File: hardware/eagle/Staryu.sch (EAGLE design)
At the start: 28 parts, among them SW1 CHERRY-MX-LED, SW2 CHERRY-MX-LED, SW3 CHERRY-MX-LED, SW4 CHERRY-MX-LED, SW5 CHERRY-MX-LED, U1 ATMEGA32U2-TQFP, Y1 16MHZ

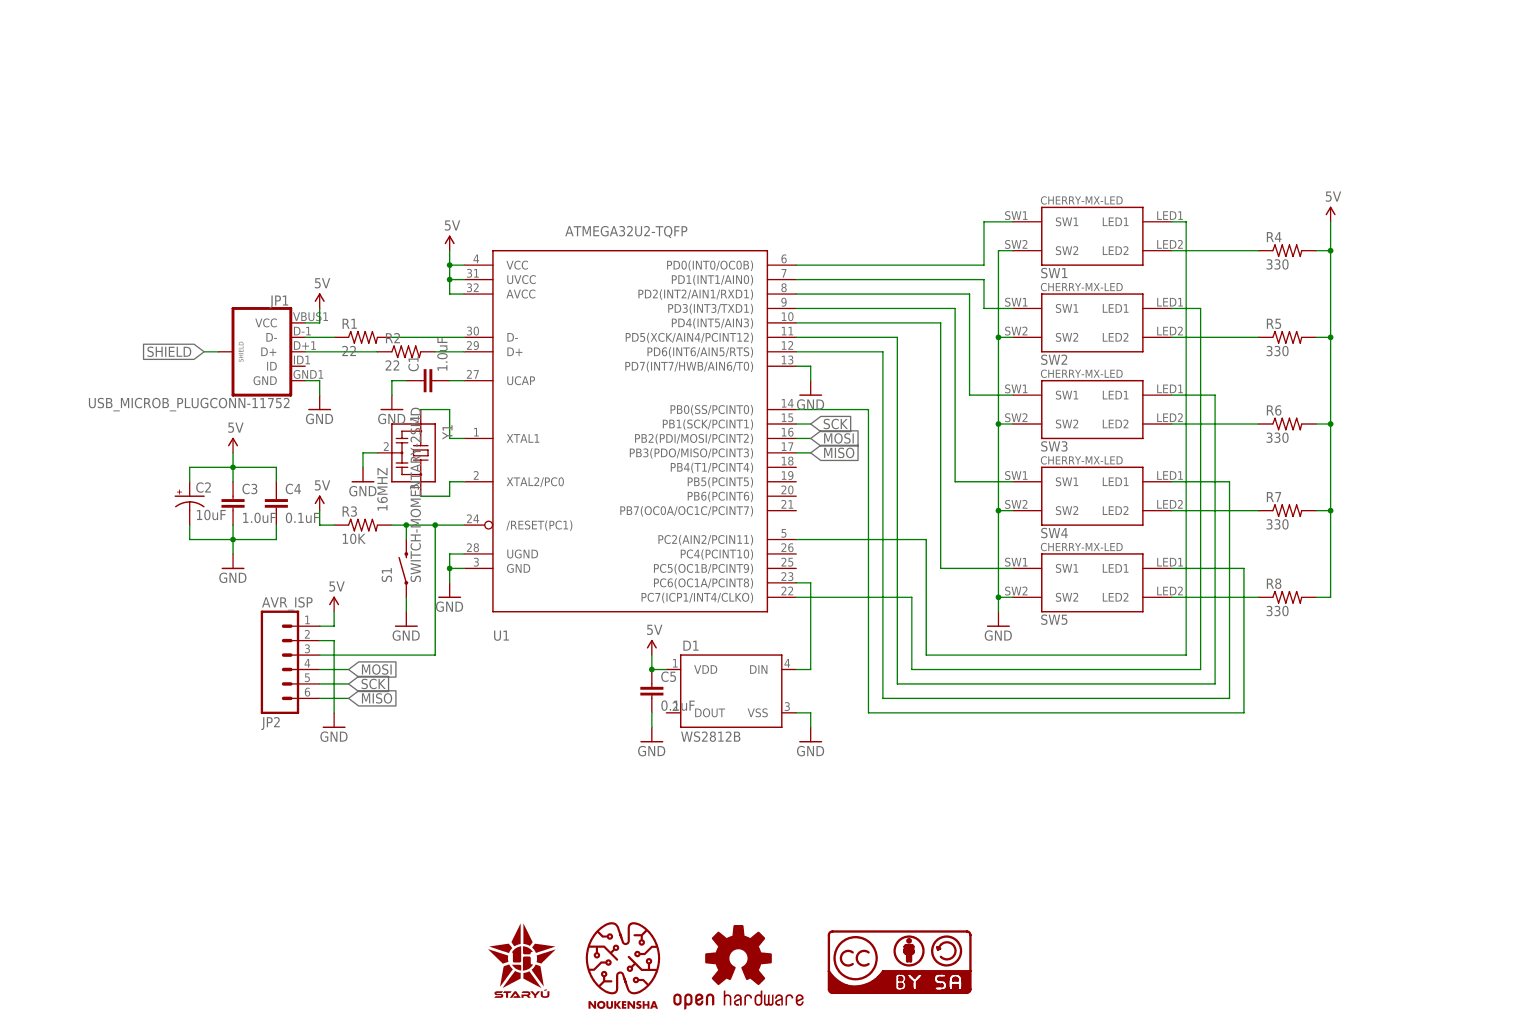
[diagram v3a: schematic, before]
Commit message: Update hardware to v1.4 - Support both of ATMEGA32U2-AU (32-TQFP) and ATMEGA32U2-MU (32-QFN) - Support both of normal and reverse mounting switch (selected by jumper) - Replace Micro USB connector with a much tougher one - Add a new DOUT connector exported from WS2812B - Correct name and value of Y1 - Change logo
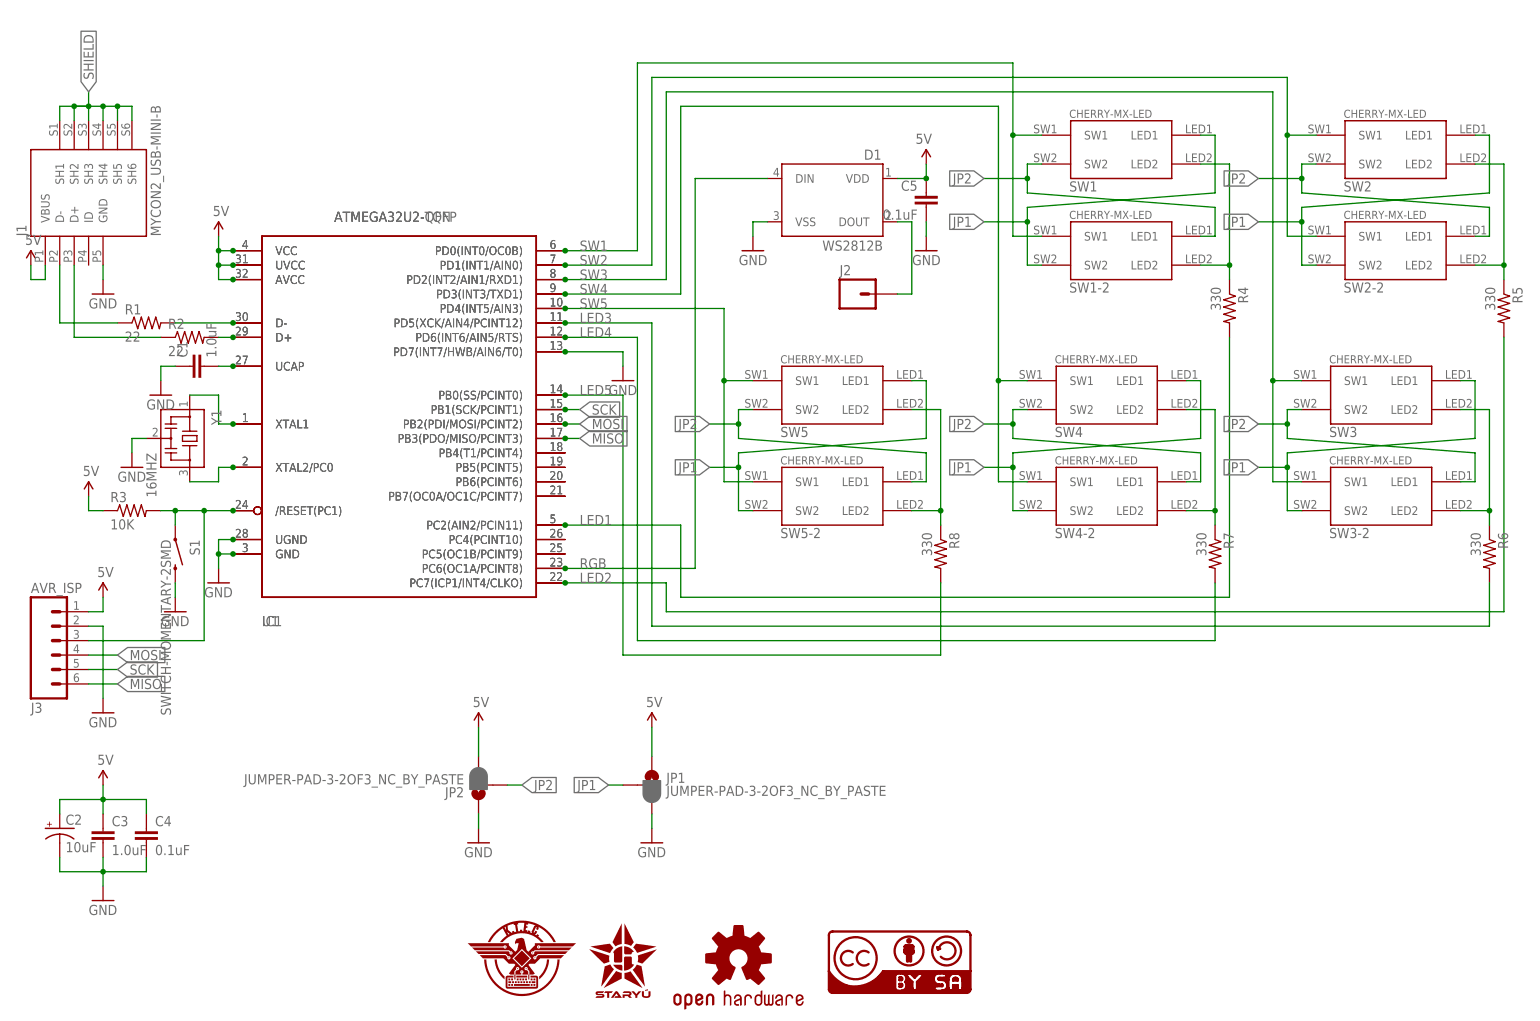
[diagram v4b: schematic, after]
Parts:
- removed LOGO2: NOUKENSHA_LOGO.3_EXP, Noukensha:NOUKENSHA_LOGO.3_EXP
- added IC1: ATMEGA32U2-QFN, atmega32u2:ATMEGA32U2-QFN
- added J1: MYCON2_USB-MINI-B, usb-micro-b:MYCON2_USB-MINI-B
- added J2: (no value), SparkFun-Connectors:M01PTH_NO_SILK_YES_STOP
- added J3: AVR_ISP, SparkFun-Connectors:M06NO_SILK_FEMALE_PTH
- added SW1-2, SW2-2, SW3-2, SW4-2, SW5-2: CHERRY-MX-LED-MOD, cherrymx:CHERRY-MX-LED-MOD
- added U$1: K.T.E.C._LOGO.3_INCH_EXP, logo:K.T.E.C._LOGO.3_INCH_EXP
- C1, C3: device SparkFun-Capacitors:CAP0805 -> SparkFun-Capacitors:1.0UF-25V-+80/-20(0805)"
- JP1: value USB_MICROB_PLUGCONN-11752 -> JUMPER-PAD-3-2OF3_NC_BY_PASTE; device SparkFun-Connectors:USB_MICROB_PLUGCONN-11752 -> SparkFun-Passives:JUMPER-PAD-3-2OF3_NC_BY_PASTE
- JP2: value AVR_ISP -> JUMPER-PAD-3-2OF3_NC_BY_PASTE; device SparkFun-Connectors:M06NO_SILK_FEMALE_PTH -> SparkFun-Passives:JUMPER-PAD-3-2OF3_NC_BY_PASTE
- SW1, SW2, SW3, SW4, SW5: value CHERRY-MX-LED -> CHERRY-MX-LED-MOD; device cherrymx:CHERRY-MX-LED -> cherrymx:CHERRY-MX-LED-MOD
- U1: device adafruit:ATMEGA32U2-TQFP -> atmega32u2:ATMEGA32U2-TQFP
- Y1: device cstce-resonator:CSTCR6M00G53Z -> cst-resonator:CSTCE16M0V53-R0
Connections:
- removed net N$14: SW1.SW1, U1.PD0(INT0/OC0B)
- removed net N$15: SW2.SW1, U1.PD1(INT1/AIN0)
- removed net N$16: SW3.SW1, U1.PD2(INT2/AIN1/RXD1)
- removed net N$17: SW4.SW1, U1.PD3(INT3/TXD1)
- removed net N$18: SW5.SW1, U1.PD4(INT5/AIN3)
- removed net N$19: D1.DIN, U1.PC6(OC1A/PCINT8)
- removed net N$30: SW4.LED1, U1.PD6(INT6/AIN5/RTS)
- removed net N$31: SW2.LED1, U1.PC7(ICP1/INT4/CLKO)
- removed net N$32: SW3.LED1, U1.PD5(XCK/AIN4/PCINT12)
- removed net N$33: SW5.LED1, U1.PB0(SS/PCINT0)
- removed net N$34: SW1.LED1, U1.PC2(AIN2/PCIN11)
- new net JP1: JP1.2, SW1-2.SW2, SW1.LED1, SW2-2.SW2, SW2.LED1, SW3-2.SW2, SW3.LED1, SW4-2.SW2, SW4.LED1, SW5-2.SW2, SW5.LED1
- new net JP2: JP2.2, SW1-2.LED1, SW1.SW2, SW2-2.LED1, SW2.SW2, SW3-2.LED1, SW3.SW2, SW4-2.LED1, SW4.SW2, SW5-2.LED1, SW5.SW2
- new net LED1: IC1.PC2(AIN2/PCIN11), R4.2, U1.PC2(AIN2/PCIN11)
- new net LED2: IC1.PC7(ICP1/INT4/CLKO), R5.2, U1.PC7(ICP1/INT4/CLKO)
- new net LED3: IC1.PD5(XCK/AIN4/PCINT12), R6.2, U1.PD5(XCK/AIN4/PCINT12)
- new net LED4: IC1.PD6(INT6/AIN5/RTS), R7.2, U1.PD6(INT6/AIN5/RTS)
- new net LED5: IC1.PB0(SS/PCINT0), R8.2, U1.PB0(SS/PCINT0)
- new net N$20: IC1.PB4(T1/PCINT4), U1.PB4(T1/PCINT4)
- new net N$21: IC1.PB5(PCINT5), U1.PB5(PCINT5)
- new net N$22: IC1.PB6(PCINT6), U1.PB6(PCINT6)
- new net N$23: IC1.PB7(OC0A/OC1C/PCINT7), U1.PB7(OC0A/OC1C/PCINT7)
- new net N$24: IC1.PC4(PCINT10), U1.PC4(PCINT10)
- new net N$25: IC1.PC5(OC1B/PCINT9), U1.PC5(OC1B/PCINT9)
- new net N$29: R4.1, SW1-2.LED2, SW1.LED2
- new net RGB: D1.DIN, IC1.PC6(OC1A/PCINT8), U1.PC6(OC1A/PCINT8)
- new net SW1: IC1.PD0(INT0/OC0B), SW1-2.SW1, SW1.SW1, U1.PD0(INT0/OC0B)
- new net SW2: IC1.PD1(INT1/AIN0), SW2-2.SW1, SW2.SW1, U1.PD1(INT1/AIN0)
- new net SW3: IC1.PD2(INT2/AIN1/RXD1), SW3-2.SW1, SW3.SW1, U1.PD2(INT2/AIN1/RXD1)
- new net SW4: IC1.PD3(INT3/TXD1), SW4-2.SW1, SW4.SW1, U1.PD3(INT3/TXD1)
- new net SW5: IC1.PD4(INT5/AIN3), SW5-2.SW1, SW5.SW1, U1.PD4(INT5/AIN3)
- net 5V: now also IC1.AVCC, IC1.UVCC, IC1.VCC, J1.VBUS, J3.1, JP1.1, JP2.3; no longer JP1.VCC, JP2.1, R4.2, R5.2, R6.2, R7.2, R8.2
- net GND: now also IC1.GND, IC1.PD7(INT7/HWB/AIN6/T0), IC1.UGND, J1.GND, J3.2, JP1.3, JP2.1, S1.2; no longer JP1.GND, JP2.2, S1.1, SW1.SW2, SW2.SW2, SW3.SW2, SW4.SW2, SW5.SW2
- net MISO: now also IC1.PB3(PDO/MISO/PCINT3), J3.6; no longer JP2.6
- net MOSI: now also IC1.PB2(PDI/MOSI/PCINT2), J3.4; no longer JP2.4
- net N$1: now also IC1.D+
- net N$10: now also SW2-2.LED2
- net N$11: now also SW3-2.LED2
- net N$12: now also SW4-2.LED2
- net N$13: now also SW5-2.LED2
- net N$2: now also IC1.D-
- net N$3: now also J1.D-; no longer JP1.D-
- net N$4: now also J1.D+; no longer JP1.D+
- net N$5: now also IC1.XTAL1
- net N$6: now also IC1.XTAL2/PC0
- net N$7: now also IC1.UCAP
- net N$8: now also IC1./RESET(PC1), J3.3, S1.1; no longer JP2.3, S1.2
- net N$9: now also D1.DOUT, J2.1; no longer R4.1, SW1.LED2
- net SCK: now also IC1.PB1(SCK/PCINT1), J3.5; no longer JP2.5
- net SHIELD: now also J1.SH1, J1.SH2, J1.SH3, J1.SH4, J1.SH5, J1.SH6; no longer JP1.SHIELD
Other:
- moved on the sheet: C1, C2, C3, C4, C5, D1, R1, R2, R3, R4, R5, R6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

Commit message: Update hardware to v1.5 - Improve jumpers for selecting switch mounting - Change logo
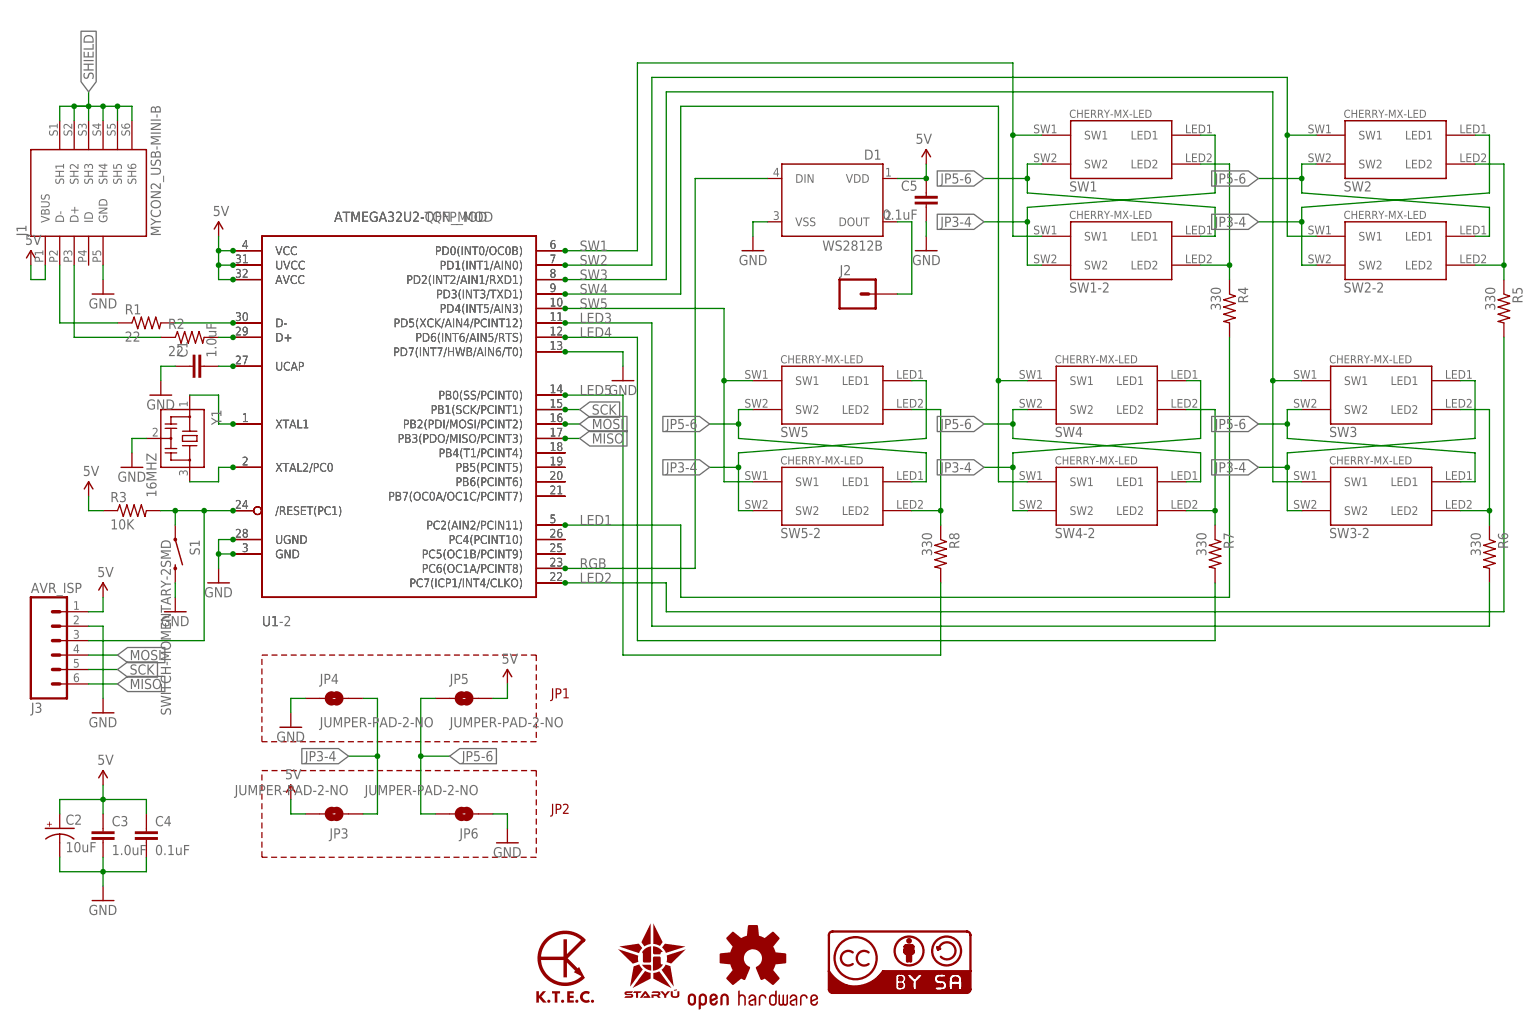
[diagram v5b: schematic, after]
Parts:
- removed IC1: ATMEGA32U2-QFN, atmega32u2:ATMEGA32U2-QFN
- removed JP1, JP2: JUMPER-PAD-3-2OF3_NC_BY_PASTE, SparkFun-Passives:JUMPER-PAD-3-2OF3_NC_BY_PASTE
- removed U$1: K.T.E.C._LOGO.3_INCH_EXP, logo:K.T.E.C._LOGO.3_INCH_EXP
- added JP3, JP4, JP5, JP6: JUMPER-PAD-2-NO, SparkFun-Passives:JUMPER-PAD-2-NO
- added LOGO2: STARYU_LOGO, Noukensha:STARYU_LOGO
- added U1-2: ATMEGA32U2-QFN_MOD, atmega32u2:ATMEGA32U2-QFN_MOD
- LOGO1: value STARYU_LOGO -> K.T.E.C._LOGO3_COPPER_EXP_S; device Noukensha:STARYU_LOGO -> logo:K.T.E.C._LOGO3_COPPER_EXP_S
- U1: value ATMEGA32U2-TQFP -> ATMEGA32U2-TQFP_MOD; device atmega32u2:ATMEGA32U2-TQFP -> atmega32u2:ATMEGA32U2-TQFP_MOD
- renumbered U$3 to LOGO4
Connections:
- removed net JP1: JP1.2, SW1-2.SW2, SW1.LED1, SW2-2.SW2, SW2.LED1, SW3-2.SW2, SW3.LED1, SW4-2.SW2, SW4.LED1, SW5-2.SW2, SW5.LED1
- removed net JP2: JP2.2, SW1-2.LED1, SW1.SW2, SW2-2.LED1, SW2.SW2, SW3-2.LED1, SW3.SW2, SW4-2.LED1, SW4.SW2, SW5-2.LED1, SW5.SW2
- new net JP3-4: JP3.1, JP4.2, SW1-2.SW2, SW1.LED1, SW2-2.SW2, SW2.LED1, SW3-2.SW2, SW3.LED1, SW4-2.SW2, SW4.LED1, SW5-2.SW2, SW5.LED1
- new net JP5-6: JP5.1, JP6.2, SW1-2.LED1, SW1.SW2, SW2-2.LED1, SW2.SW2, SW3-2.LED1, SW3.SW2, SW4-2.LED1, SW4.SW2, SW5-2.LED1, SW5.SW2
- net 5V: now also JP3.2, JP5.2, U1-2.AVCC, U1-2.UVCC, U1-2.VCC; no longer IC1.AVCC, IC1.UVCC, IC1.VCC, JP1.1, JP2.3
- net GND: now also JP4.1, JP6.1, U1-2.GND, U1-2.PD7(INT7/HWB/AIN6/T0), U1-2.UGND; no longer IC1.GND, IC1.PD7(INT7/HWB/AIN6/T0), IC1.UGND, JP1.3, JP2.1
- net LED1: now also U1-2.PC2(AIN2/PCIN11); no longer IC1.PC2(AIN2/PCIN11)
- net LED2: now also U1-2.PC7(ICP1/INT4/CLKO); no longer IC1.PC7(ICP1/INT4/CLKO)
- net LED3: now also U1-2.PD5(XCK/AIN4/PCINT12); no longer IC1.PD5(XCK/AIN4/PCINT12)
- net LED4: now also U1-2.PD6(INT6/AIN5/RTS); no longer IC1.PD6(INT6/AIN5/RTS)
- net LED5: now also U1-2.PB0(SS/PCINT0); no longer IC1.PB0(SS/PCINT0)
- net MISO: now also U1-2.PB3(PDO/MISO/PCINT3); no longer IC1.PB3(PDO/MISO/PCINT3)
- net MOSI: now also U1-2.PB2(PDI/MOSI/PCINT2); no longer IC1.PB2(PDI/MOSI/PCINT2)
- net N$1: now also U1-2.D+; no longer IC1.D+
- net N$2: now also U1-2.D-; no longer IC1.D-
- net N$20: now also U1-2.PB4(T1/PCINT4); no longer IC1.PB4(T1/PCINT4)
- net N$21: now also U1-2.PB5(PCINT5); no longer IC1.PB5(PCINT5)
- net N$22: now also U1-2.PB6(PCINT6); no longer IC1.PB6(PCINT6)
- net N$23: now also U1-2.PB7(OC0A/OC1C/PCINT7); no longer IC1.PB7(OC0A/OC1C/PCINT7)
- net N$24: now also U1-2.PC4(PCINT10); no longer IC1.PC4(PCINT10)
- net N$25: now also U1-2.PC5(OC1B/PCINT9); no longer IC1.PC5(OC1B/PCINT9)
- net N$5: now also U1-2.XTAL1; no longer IC1.XTAL1
- net N$6: now also U1-2.XTAL2/PC0; no longer IC1.XTAL2/PC0
- net N$7: now also U1-2.UCAP; no longer IC1.UCAP
- net N$8: now also U1-2./RESET(PC1); no longer IC1./RESET(PC1)
- net RGB: now also U1-2.PC6(OC1A/PCINT8); no longer IC1.PC6(OC1A/PCINT8)
- net SCK: now also U1-2.PB1(SCK/PCINT1); no longer IC1.PB1(SCK/PCINT1)
- net SW1: now also U1-2.PD0(INT0/OC0B); no longer IC1.PD0(INT0/OC0B)
- net SW2: now also U1-2.PD1(INT1/AIN0); no longer IC1.PD1(INT1/AIN0)
- net SW3: now also U1-2.PD2(INT2/AIN1/RXD1); no longer IC1.PD2(INT2/AIN1/RXD1)
- net SW4: now also U1-2.PD3(INT3/TXD1); no longer IC1.PD3(INT3/TXD1)
- net SW5: now also U1-2.PD4(INT5/AIN3); no longer IC1.PD4(INT5/AIN3)
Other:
- note added: "JP1"
- note added: "JP2"
